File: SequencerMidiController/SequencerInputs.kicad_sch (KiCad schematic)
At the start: 36 parts, among them SW10 SW_SPST, SW4 SW_SPST, SW5 SW_SPST, SW6 SW_SPST, SW8 SW_SPST, SW9 SW_SPST, U35 ADP5587-ACPZ_LFCSP24, U36 TLC5955DCA_HTSSOP56, U37 TLC5955DCA_HTSSOP56

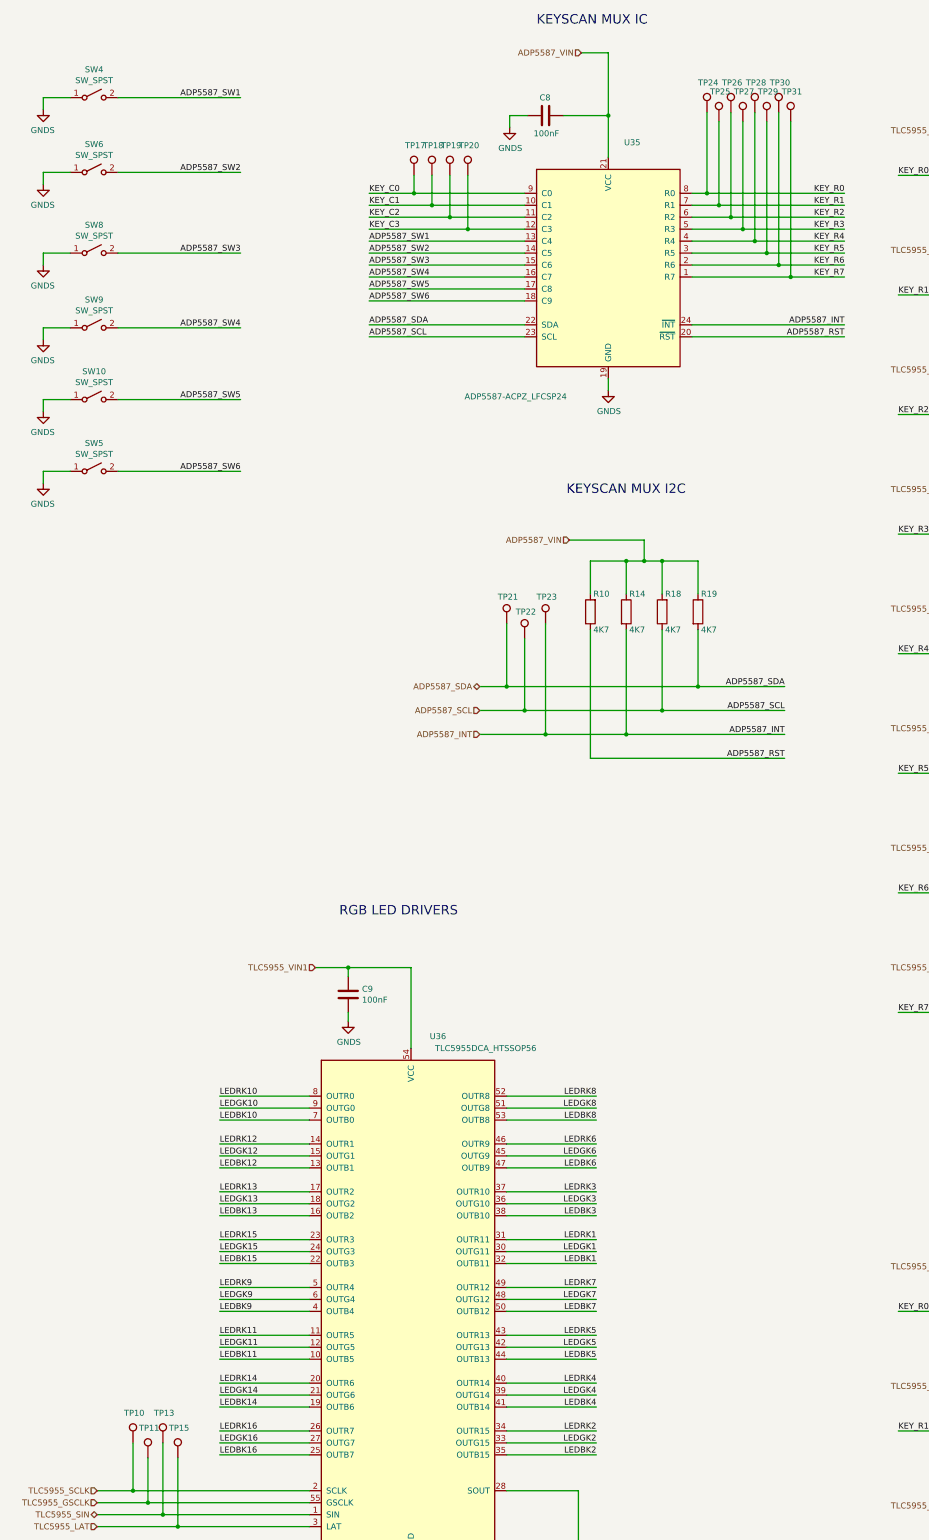
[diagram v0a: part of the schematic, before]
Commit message: Add ground points
https://github.com/cracked-machine/BassStationSequencerMidiController/issues/9

Also, made space on layout for uSDCard IDC connector and DAC analog output section
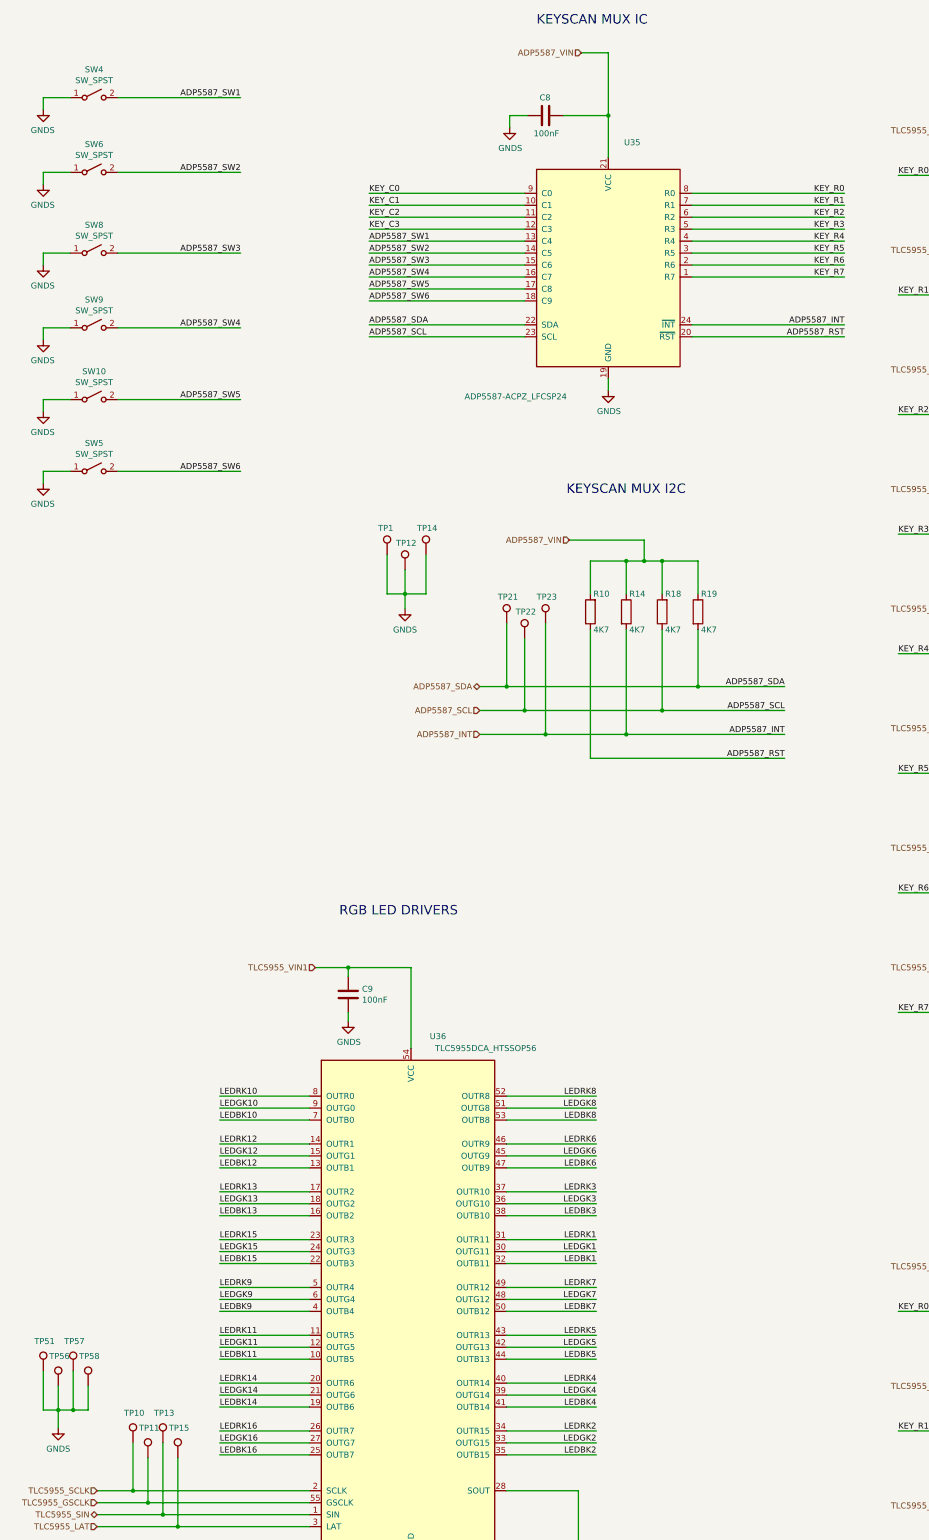
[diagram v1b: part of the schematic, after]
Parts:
- removed TP17, TP18, TP19, TP20, TP24, TP25, TP26, TP27, TP28, TP29, TP30, TP31: TestPoint, TestPoint:TestPoint_Pad_D1.0mm, symbol Connector:TestPoint
- added TP1, TP12, TP14, TP51, TP56, TP57, TP58: TestPoint, TestPoint:TestPoint_Pad_D1.0mm, symbol Connector:TestPoint
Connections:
- net GNDS: now also TP1.1, TP12.1, TP14.1, TP51.1, TP56.1, TP57.1, TP58.1
